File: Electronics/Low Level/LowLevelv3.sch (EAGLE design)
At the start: 71 parts, among them IC1_2515 MCP2515, IC2_2551 MCP2551DIL08, IC3_4802 MCP4802, Q1 16MHz, T1 2N3904, T2 2N3904, X1 284512-4, X3 Motor, X4 CLICK

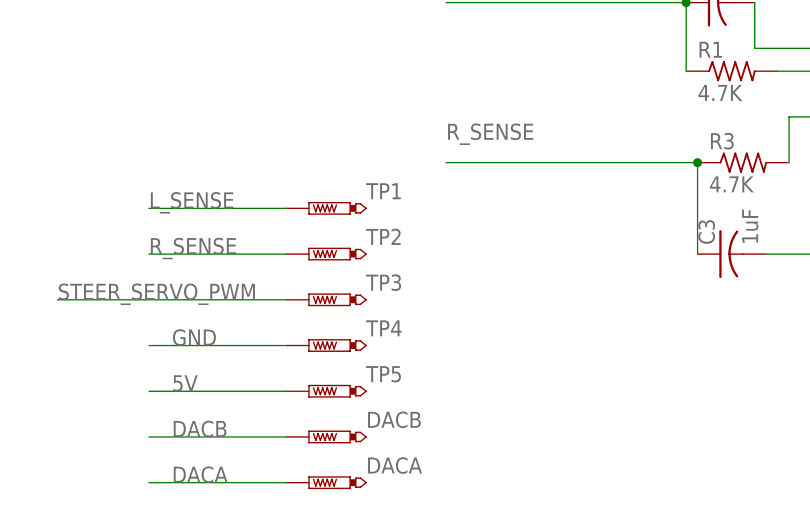
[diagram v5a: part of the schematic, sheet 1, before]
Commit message: Minorsilkscreen updates
Named testpoints
Swapped 10k for 0 ohm resistor on reset button
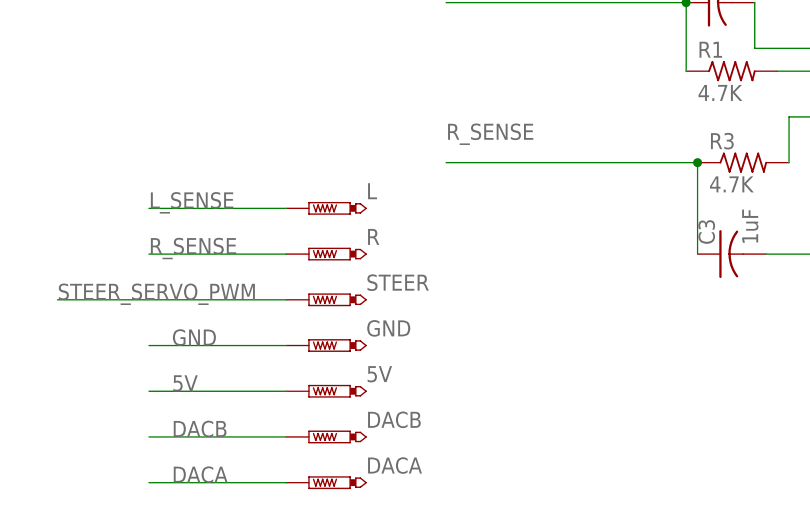
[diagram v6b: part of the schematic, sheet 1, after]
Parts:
- R11: value 10k -> 0
- renumbered TP1 to L, TP2 to R, TP3 to STEER, TP4 to GND, TP5 to 5V
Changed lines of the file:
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@@
 <part name="FRAME2" library="frames" library_urn="urn:adsk.eagle:library:229" deviceset="A4L-LOC" device=""/>
 <part name="RESET" library="SparkFun-Switches" library_urn="urn:adsk.eagle:library:535" deviceset="MOMENTARY-SWITCH-SPST" device="-PTH-6.0MM" package3d_urn="urn:adsk.eagle:package:40163/1"/>
-<part name="R11" library="resistor" library_urn="urn:adsk.eagle:library:348" deviceset="R-US_" device="R1206" package3d_urn="urn:adsk.eagle:package:23540/2" value="10k"/>
+<part name="R11" library="resistor" library_urn="urn:adsk.eagle:library:348" deviceset="R-US_" device="R1206" package3d_urn="urn:adsk.eagle:package:23540/2" value="0"/>
 <part name="C12" library="resistor" library_urn="urn:adsk.eagle:library:348" deviceset="C-US" device="C1206" package3d_urn="urn:adsk.eagle:package:23618/2" value="0.1uF"/>
 <part name="C14" library="resistor" library_urn="urn:adsk.eagle:library:348" deviceset="C-US" device="C1206" package3d_urn="urn:adsk.eagle:package:23618/2" value="0.1uF"/>
@@
 <part name="R12" library="resistor" library_urn="urn:adsk.eagle:library:348" deviceset="R-US_" device="R1206" package3d_urn="urn:adsk.eagle:package:23540/2" value="1K"/>
 <part name="STEERING" library="elcanoParts" deviceset="RJ45" device="" package3d_urn="urn:adsk.eagle:package:10660/1" technology="-8L-B"/>
-<part name="TP1" library="testpad" library_urn="urn:adsk.eagle:library:385" deviceset="PTR1" device="PAD1-17" package3d_urn="urn:adsk.eagle:package:27949/1"/>
-<part name="TP2" library="testpad" library_urn="urn:adsk.eagle:library:385" deviceset="PTR1" device="PAD1-17" package3d_urn="urn:adsk.eagle:package:27949/1"/>
-<part name="TP3" library="testpad" library_urn="urn:adsk.eagle:library:385" deviceset="PTR1" device="PAD1-17" package3d_urn="urn:adsk.eagle:package:27949/1"/>
-<part name="TP4" library="testpad" library_urn="urn:adsk.eagle:library:385" deviceset="PTR1" device="PAD1-17" package3d_urn="urn:adsk.eagle:package:27949/1"/>
-<part name="TP5" library="testpad" library_urn="urn:adsk.eagle:library:385" deviceset="PTR1" device="PAD1-17" package3d_urn="urn:adsk.eagle:package:27949/1"/>
+<part name="L" library="testpad" library_urn="urn:adsk.eagle:library:385" deviceset="PTR1" device="PAD1-17" package3d_urn="urn:adsk.eagle:package:27949/1"/>
+<part name="R" library="testpad" library_urn="urn:adsk.eagle:library:385" deviceset="PTR1" device="PAD1-17" package3d_urn="urn:adsk.eagle:package:27949/1"/>
+<part name="STEER" library="testpad" library_urn="urn:adsk.eagle:library:385" deviceset="PTR1" device="PAD1-17" package3d_urn="urn:adsk.eagle:package:27949/1"/>
+<part name="GND" library="testpad" library_urn="urn:adsk.eagle:library:385" deviceset="PTR1" device="PAD1-17" package3d_urn="urn:adsk.eagle:package:27949/1"/>
+<part name="5V" library="testpad" library_urn="urn:adsk.eagle:library:385" deviceset="PTR1" device="PAD1-17" package3d_urn="urn:adsk.eagle:package:27949/1"/>
 <part name="DEBUG" library="led" library_urn="urn:adsk.eagle:library:259" deviceset="LED" device="3MM" package3d_urn="urn:adsk.eagle:package:15797/1"/>
 <part name="R2" library="resistor" library_urn="urn:adsk.eagle:library:348" deviceset="R-US_" device="R1206" package3d_urn="urn:adsk.eagle:package:23540/2" value="1K"/>
@@
 <attribute name="VALUE" x="236.22" y="32.512" size="1.778" layer="96"/>
 </instance>
-<instance part="TP1" gate="G$1" x="139.7" y="35.56" smashed="yes" rot="R90">
+<instance part="L" gate="G$1" x="139.7" y="35.56" smashed="yes" rot="R90">
 <attribute name="NAME" x="146.05" y="36.576" size="1.778" layer="95"/>
 <attribute name="TP_SIGNAL_NAME" x="142.24" y="36.83" size="1.778" layer="97" rot="R90"/>
 </instance>
-<instance part="TP2" gate="G$1" x="139.7" y="30.48" smashed="yes" rot="R90">
+<instance part="R" gate="G$1" x="139.7" y="30.48" smashed="yes" rot="R90">
 <attribute name="NAME" x="146.05" y="31.496" size="1.778" layer="95"/>
 <attribute name="TP_SIGNAL_NAME" x="142.24" y="31.75" size="1.778" layer="97" rot="R90"/>
 </instance>
-<instance part="TP3" gate="G$1" x="139.7" y="25.4" smashed="yes" rot="R90">
+<instance part="STEER" gate="G$1" x="139.7" y="25.4" smashed="yes" rot="R90">
 <attribute name="NAME" x="146.05" y="26.416" size="1.778" layer="95"/>
 <attribute name="TP_SIGNAL_NAME" x="142.24" y="26.67" size="1.778" layer="97" rot="R90"/>
 </instance>
-<instance part="TP4" gate="G$1" x="139.7" y="20.32" smashed="yes" rot="R90">
+<instance part="GND" gate="G$1" x="139.7" y="20.32" smashed="yes" rot="R90">
 <attribute name="NAME" x="146.05" y="21.336" size="1.778" layer="95"/>
 <attribute name="TP_SIGNAL_NAME" x="142.24" y="21.59" size="1.778" layer="97" rot="R90"/>
 </instance>
-<instance part="TP5" gate="G$1" x="139.7" y="15.24" smashed="yes" rot="R90">
+<instance part="5V" gate="G$1" x="139.7" y="15.24" smashed="yes" rot="R90">
 <attribute name="NAME" x="146.05" y="16.256" size="1.778" layer="95"/>
 <attribute name="TP_SIGNAL_NAME" x="142.24" y="16.51" size="1.778" layer="97" rot="R90"/>
@@
 </segment>
 <segment>
-<pinref part="TP5" gate="G$1" pin="TP"/>
+<pinref part="5V" gate="G$1" pin="TP"/>
 <wire x1="137.16" y1="15.24" x2="121.92" y2="15.24" width="0.1524" layer="91"/>
 <label x="124.46" y="15.24" size="1.778" layer="95"/>
@@
 </segment>
 <segment>
-<pinref part="TP4" gate="G$1" pin="TP"/>
+<pinref part="GND" gate="G$1" pin="TP"/>
 <wire x1="137.16" y1="20.32" x2="121.92" y2="20.32" width="0.1524" layer="91"/>
 <label x="124.46" y="20.32" size="1.778" layer="95"/>
@@
 </segment>
 <segment>
-<pinref part="TP3" gate="G$1" pin="TP"/>
+<pinref part="STEER" gate="G$1" pin="TP"/>
 <wire x1="137.16" y1="25.4" x2="111.76" y2="25.4" width="0.1524" layer="91"/>
 <label x="111.76" y="25.4" size="1.778" layer="95"/>
@@
 </segment>
 <segment>
-<pinref part="TP2" gate="G$1" pin="TP"/>
+<pinref part="R" gate="G$1" pin="TP"/>
 <wire x1="137.16" y1="30.48" x2="121.92" y2="30.48" width="0.1524" layer="91"/>
 <label x="121.92" y="30.48" size="1.778" layer="95"/>
@@
 </segment>
 <segment>
-<pinref part="TP1" gate="G$1" pin="TP"/>
+<pinref part="L" gate="G$1" pin="TP"/>
 <wire x1="137.16" y1="35.56" x2="121.92" y2="35.56" width="0.1524" layer="91"/>
 <label x="121.92" y="35.56" size="1.778" layer="95"/>
